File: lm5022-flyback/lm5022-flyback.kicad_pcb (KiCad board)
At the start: 2 copper layers, 80 x 80 mm, 55 parts, among them Q1 EPC2302, SW1 SW_Nidec_CAS-120A1, T1 Arthur, U1 LM5022MM, U2 TLVH431BQDCKT, U3 LTV-817-C

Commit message: layout work
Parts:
- removed TP15: 5004, TestPoint:TestPoint_Keystone_5000-5004_Miniature
- added REF**: Symbol_HighVoltage_Triangle_8x7mm_Copper, Symbol:Symbol_HighVoltage_Triangle_8x7mm_Copper, F.Cu at (123.0, 104.0)
- C1, C2, C5, C9, R3, R4: footprint Capacitor_SMD:C_0603_1608Metric -> Capacitor_SMD:C_0402_1005Metric
- C8: value 100pF DNP -> 100pF
- D3: value V40D103C-M3/I -> PPH10100; footprint TO_SOT_SMD_Custom:TO-263-2_Diode -> Package_TO_SOT_SMD:TO-277A
- R16: footprint Resistor_SMD:R_0603_1608Metric -> Resistor_SMD:R_0402_1005Metric; moved to B.Cu
- R2: footprint Resistor_SMD:R_2512_6332Metric -> Resistor_SMD:R_1225_3264Metric
- R8: footprint Resistor_SMD:R_0603_1608Metric -> Resistor_SMD:R_0402_1005Metric
- TP12: value 5004 -> ~; footprint TestPoint:TestPoint_Keystone_5000-5004_Miniature -> TestPoint:TestPoint_Pad_D1.0mm
- moved SW1 70.2 mm to (64.5, 91.8)
- moved R13 67.0 mm to (70.8, 80.6), turned to -90 degrees
- moved R5 66.7 mm to (68.8, 80.6), turned to -90 degrees
- moved C10 66.4 mm to (76.6, 81.2), turned to -90 degrees
- moved C6 65.2 mm to (73.4, 81.2), turned to -90 degrees
- moved Q1 61.9 mm to (81.2, 91.5)
- moved D3 58.1 mm to (73.4, 86.4), turned to -90 degrees
- moved R15 57.7 mm to (68.0, 88.6), turned to -90 degrees
- moved H3 57.4 mm to (60.5, 75.0)
- moved H5 57.4 mm to (60.5, 85.0)
- moved R14 57.1 mm to (68.6, 91.8), turned to 180 degrees
- moved R8 52.3 mm to (69.4, 93.2), turned to 180 degrees
- moved H4 51.6 mm to (60.5, 105.0)
- moved R16 51.4 mm to (74.2, 93.2), turned to -90 degrees
- moved TP12 50.2 mm to (76.0, 90.2)
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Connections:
- net Net-(Q1-S-Pad2) renamed /VS
- C10 pad 2: Net-(D3-K) -> /VSN
- C6 pad 2: Net-(D3-K) -> /VSN
- D3 pad 1: Net-(D3-K) -> /VD
- D3 pad 2: Net-(D3-A) -> /VD
- Q1 pad 3: Net-(D3-A) -> /VD
- Q1 pad 5: Net-(D3-A) -> /VD
- Q1 pad 7: Net-(D3-A) -> /VD
- R13 pad 2: Net-(D3-K) -> /VSN
- R5 pad 2: Net-(D3-K) -> /VSN
- T1 pad 2: Net-(D3-A) -> /VD
- TP1 pad 1: Net-(D3-K) -> /VSN
- TP3 pad 1: Net-(D3-A) -> /VD
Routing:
- net +BATT: track 0.00 -> 13.9 mm
- net Net-(SW1-C): track 0.00 -> 10.3 mm
- net GND: track 0.00 -> 7.28 mm
- net /VS: track 0.00 -> 7.18 mm
- net Net-(U1-CS): track 0.00 -> 4.71 mm
- net Net-(U1-OUT): track 0.00 -> 3.74 mm
- net Net-(C1-Pad1): track 0.00 -> 2.04 mm
- net Net-(U1-VCC): track 0.00 -> 1.78 mm
- net Net-(U1-SS): track 0.00 -> 1.77 mm
- net Net-(U1-RT): track 0.00 -> 1.62 mm
- net +6V: track 0.00 -> 1.47 mm
- net Net-(Q1-G): track 0.00 -> 1.35 mm
- added copper zone on F.Cu, net +BATT
- added copper zone on F.Cu, net /VD
- added copper zone on F.Cu, net /VS
- added copper zone on F.Cu, net /VSN
- added copper zone on B.Cu, net GND
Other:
- board size 80 x 80 mm -> 75.2 x 40.6 mm
- board text added: "-400V"
- board text added: "6VDRV"
- board text added: "DANGER: HIGH VOLTAGE 400V OUTPUT REQUIRES 200uF BULK OUTPUT CAPACITANCE OR CV LOAD"
- board text added: "HVGND"
- board text added: "LVGND"
- board text added: "VIN"

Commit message: finish layout
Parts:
- removed TP4: 5004, TestPoint:TestPoint_Keystone_5000-5004_Miniature
- added C11: 22uF, Capacitor_SMD:C_1210_3225Metric, F.Cu at (76.7, 72.2)
- added C12: 22uF, Capacitor_SMD:C_1210_3225Metric, F.Cu at (73.0, 72.2)
- moved H5 12.0 mm to (60.5, 97.0)
- moved R9 6.00 mm to (94.6, 101.0)
- moved REF** 4.23 mm to (127.2, 104.2)
- moved TP8 3.50 mm to (101.6, 104.7)
- moved C7 3.00 mm to (106.6, 105.0)
- moved C8 3.00 mm to (88.8, 105.6)
- moved D2 3.00 mm to (105.6, 108.6)
- moved R6 3.00 mm to (108.2, 107.8)
- moved TP10 3.00 mm to (113.4, 107.0)
- moved TP13 3.00 mm to (86.2, 104.6)
- moved TP14 3.00 mm to (86.2, 108.2)
- moved TP9 3.00 mm to (101.6, 108.2)
- moved U2 3.00 mm to (109.3, 105.0)
- moved U3 3.00 mm to (98.4, 106.9)
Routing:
- net +6V: track 1.47 -> 49.4 mm, vias 0 -> 2
- net -400V: track 0.00 -> 40.5 mm, vias 0 -> 3
- net Net-(D2-K): track 0.00 -> 37.4 mm
- net Net-(C8-Pad1): track 0.00 -> 19.2 mm
- net Net-(U2-REF): track 0.00 -> 17.4 mm
- net /FB: track 0.00 -> 12.6 mm, vias 0 -> 2
- net Net-(U2-K): track 0.00 -> 10.5 mm
- net Net-(U1-COMP): track 0.00 -> 1.56 mm, vias 0 -> 1
- net GND: track 7.28 -> 8.24 mm, vias 0 -> 102
- added copper zone on F.Cu, net -400V
- added copper zone on F.Cu, net GND
- added copper zone on F.Cu, net HVGND
- added copper zone on F.Cu, net Net-(D1-K)
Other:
- board size 75.2 x 40.6 mm -> 75.9 x 43.6 mm
- board text added: "APEx -400V Flyback Converter Rev 1.0 Alan Hsu"

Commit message: Flyback Rev 1.0 release
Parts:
- R15: footprint Capacitor_SMD:C_0603_1608Metric -> Resistor_SMD:R_0603_1608Metric
- TP7: value TestPoint -> 5004
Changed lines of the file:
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@@
 			(outputformat 1)
 			(mirror no)
-			(drillshape 1)
+			(drillshape 0)
 			(scaleselection 1)
-			(outputdirectory "")
+			(outputdirectory "Outputs/")
 		)
 	)
@@
 		)
 	)
-	(footprint "Capacitor_SMD:C_0603_1608Metric"
+	(footprint "Resistor_SMD:R_0603_1608Metric"
 		(layer "F.Cu")
 		(at 68 88.6 -90)
-		(descr "Capacitor SMD 0603 (1608 Metric), square (rectangular) end terminal, IPC-7351 nominal, (Body size source: IPC-SM-782 page 76, https://www.pcb-3d.com/wordpress/wp-content/uploads/ipc-sm-782a_amendment_1_and_2.pdf), generated with kicad-footprint-generator")
-		(tags "capacitor")
+		(descr "Resistor SMD 0603 (1608 Metric), square (rectangular) end terminal, IPC-7351 nominal, (Body size source: IPC-SM-782 page 72, https://www.pcb-3d.com/wordpress/wp-content/uploads/ipc-sm-782a_amendment_1_and_2.pdf), generated with kicad-footprint-generator")
+		(tags "resistor")
 		(property "Reference" "R15"
-			(at 0 -1.2 90)
+			(at 0 1.2 270)
 			(layer "F.SilkS")
 			(effects
@@
 		)
 		(property "Value" "33K"
-			(at 0 1.43 90)
+			(at 0 1.43 270)
 			(layer "F.Fab")
 			(effects
@@
 		)
 		(property "Datasheet" "~"
-			(at 0 0 90)
+			(at 0 0 270)
 			(layer "F.Fab")
 			(hide yes)
@@
 		)
 		(property "Description" "Resistor"
-			(at 0 0 90)
+			(at 0 0 270)
 			(layer "F.Fab")
 			(hide yes)
@@
 		(attr smd)
 		(fp_line
-			(start -0.14058 0.51)
-			(end 0.14058 0.51)
+			(start -0.237258 0.5225)
+			(end 0.237258 0.5225)
 			(stroke
 				(width 0.12)
@@
 		)
 		(fp_line
-			(start -0.14058 -0.51)
-			(end 0.14058 -0.51)
+			(start -0.237258 -0.5225)
+			(end 0.237258 -0.5225)
 			(stroke
 				(width 0.12)
@@
 		)
 		(fp_rect
-			(start -0.8 -0.4)
-			(end 0.8 0.4)
+			(start -0.8 -0.4125)
+			(end 0.8 0.4125)
 			(stroke
 				(width 0.1)
@@
 		)
 		(fp_text user "${REFERENCE}"
-			(at 0 0 90)
+			(at 0 0 270)
 			(layer "F.Fab")
 			(effects
@@
 		)
 		(pad "1" smd roundrect
-			(at -0.775 0 270)
-			(size 0.9 0.95)
+			(at -0.825 0 270)
+			(size 0.8 0.95)
 			(layers "F.Cu" "F.Mask" "F.Paste")
 			(roundrect_rratio 0.25)
@@
 		)
 		(pad "2" smd roundrect
-			(at 0.775 0 270)
-			(size 0.9 0.95)
+			(at 0.825 0 270)
+			(size 0.8 0.95)
 			(layers "F.Cu" "F.Mask" "F.Paste")
 			(roundrect_rratio 0.25)
@@
 		)
 		(embedded_fonts no)
-		(model "${KICAD9_3DMODEL_DIR}/Capacitor_SMD.3dshapes/C_0603_1608Metric.step"
+		(model "${KICAD9_3DMODEL_DIR}/Resistor_SMD.3dshapes/R_0603_1608Metric.step"
 			(offset
 				(xyz 0 0 0)
@@
 			)
 		)
-		(property "Value" "TestPoint"
+		(property "Value" "5004"
 			(at 0 2.5 0)
 			(layer "F.Fab")

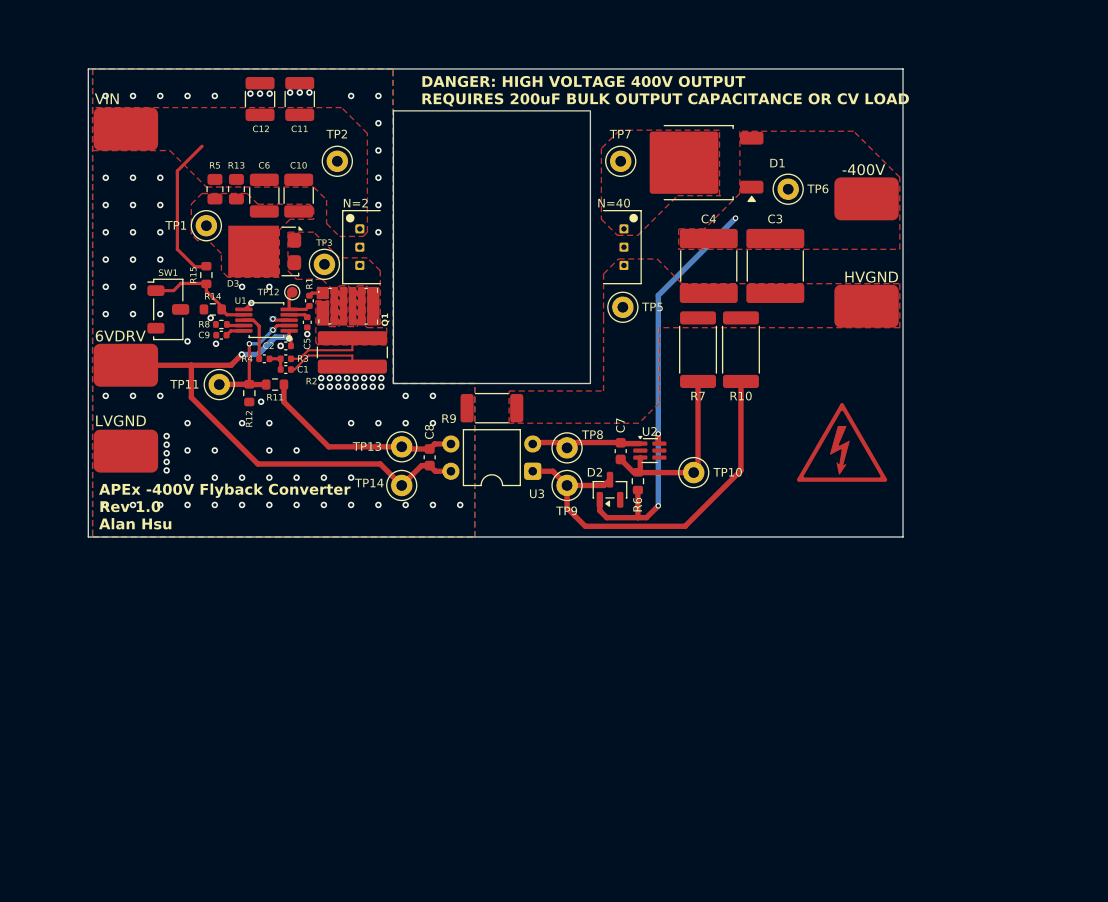
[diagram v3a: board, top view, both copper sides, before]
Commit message: rev 2 of 400V converter
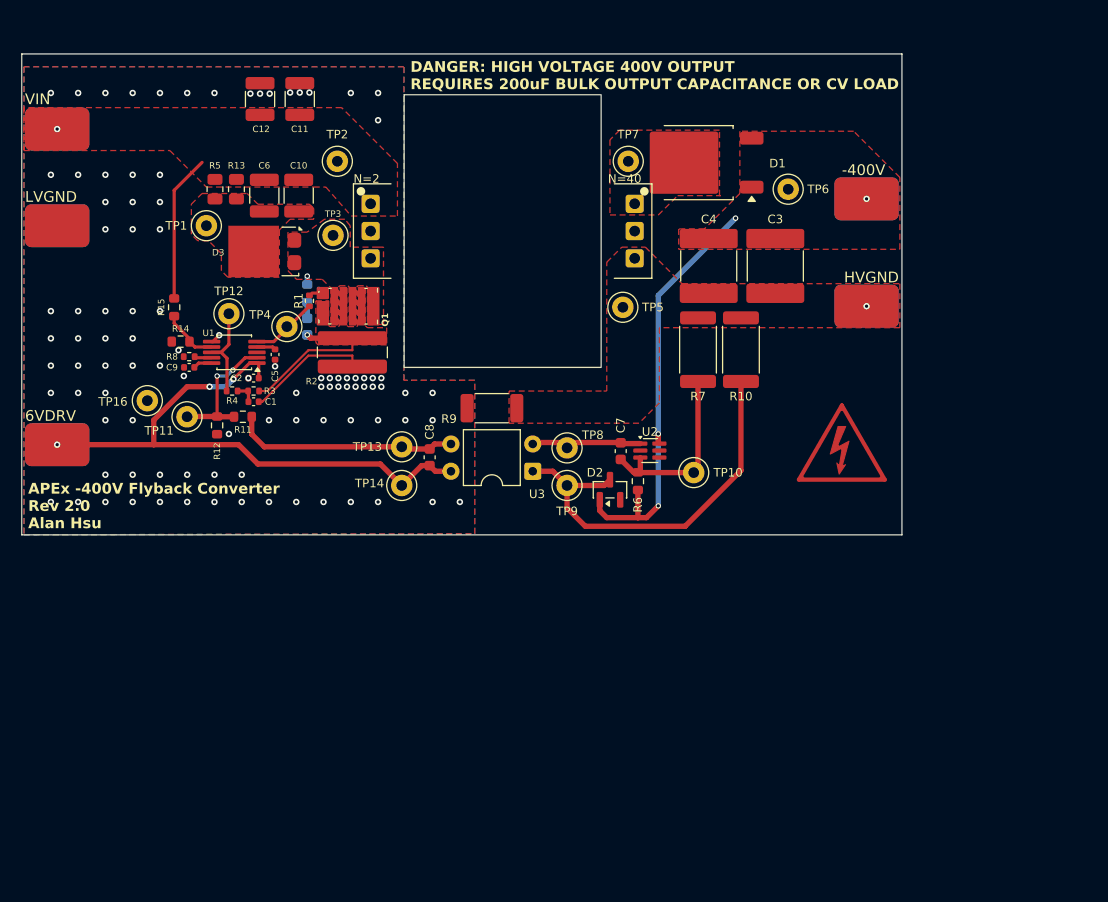
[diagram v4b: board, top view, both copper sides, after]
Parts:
- removed R16: 0R, Resistor_SMD:R_0402_1005Metric
- removed SW1: SW_Nidec_CAS-120A1, Button_Switch_SMD:Nidec_Copal_CAS-120A
- added C13: 100pF, Capacitor_SMD:C_0603_1608Metric, B.Cu at (77.4, 93.4)
- added R17: 100, Resistor_SMD:R_0603_1608Metric, B.Cu at (77.4, 90.3)
- added TP16: 5004, TestPoint:TestPoint_Keystone_5000-5004_Miniature, F.Cu at (62.5, 100.3)
- added TP4: 5004, TestPoint:TestPoint_Keystone_5000-5004_Miniature, F.Cu at (75.5, 93.4)
- D1: value VS-8EWS12STRL-M3 -> VS-8EWS16STR-M3
- R1, R3, R4: footprint Capacitor_SMD:C_0402_1005Metric -> Resistor_SMD:R_0402_1005Metric
- TP12: value ~ -> 5004; footprint TestPoint:TestPoint_Pad_D1.0mm -> TestPoint:TestPoint_Keystone_5000-5004_Miniature
- moved H4 22.0 mm to (54.1, 84.0)
- moved H5 9.78 mm to (54.1, 104.4)
- moved H3 6.40 mm to (54.1, 75.0)
- moved TP12 6.23 mm to (70.1, 92.2)
- moved C1 4.24 mm to (72.4, 100.4)
- moved C2 4.24 mm to (72.4, 98.2)
- moved C5 4.24 mm to (74.4, 96.0)
- moved C9 4.24 mm to (66.4, 97.2)
- moved R11 4.24 mm to (71.4, 101.8)
- moved R12 4.24 mm to (69.0, 102.6)
- moved R14 4.24 mm to (65.6, 94.8)
- moved R15 4.24 mm to (65.0, 91.6)
- moved R3 4.24 mm to (72.4, 99.4)
- moved R4 4.24 mm to (70.4, 99.4)
- moved R8 4.24 mm to (66.4, 96.2)
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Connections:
- TP12 pad 1: Net-(U1-OUT) -> Net-(U1-CS)
- U1 pad 3: Net-(U1-COMP) -> unconnected-(U1-COMP-Pad3)
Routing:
- net /VS: track 7.18 -> 15.7 mm, vias 0 -> 1
- net +6V: track 49.4 -> 55.6 mm, vias 2 -> 3
- net Net-(U1-UVLO): track 10.3 -> 5.28 mm
- net GND: track 8.24 -> 12.5 mm, vias 102 -> 99
- net Net-(U1-CS): track 4.71 -> 8.61 mm
- net Net-(U1-OUT): track 3.74 -> 6.26 mm
- net Net-(C8-Pad1): track 19.2 -> 20.9 mm
- net Net-(U1-COMP): track 1.56 -> 0.00 mm, vias 1 -> 0
- net Net-(C13-Pad1): track 0.00 -> 1.50 mm
- net /VD: track 0.00 -> 0.77 mm, vias 0 -> 1
- net +BATT: track 13.9 -> 13.8 mm, vias 0 -> 1
- net HVGND: vias 0 -> 1
- net -400V: vias 3 -> 4
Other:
- board size 75.9 x 43.6 mm -> 82 x 44.8 mm
- board text added: "APEx -400V Flyback Converter Rev 2.0 Alan Hsu"
- board text removed: "APEx -400V Flyback Converter Rev 1.0 Alan Hsu"
